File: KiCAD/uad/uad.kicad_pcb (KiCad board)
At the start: 2 copper layers, 100 x 70 mm, 77 parts, among them M3 ОтверстиеD3, X1 L_220, X2 N_220, X3 L_12, X4 N_12

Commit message: в общий проект добавлена лицевая панель под потенциометр
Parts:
- added G***: LOGO, N_ICO:el-nikitos_19x7, F.Cu at (116.5, 67.2)
- added M8: Отверстие_М8, N_X:Отверстие_М8, F.Cu at (95.2, 67.0)
- added XP10: Вилка_PLS3, N_X:Вилка_PLS3_угловая_вертикальная, B.Cu at (118.5, 62.2)
- added XP11: Вилка_PLS3, N_X:Вилка_PLS3_угловая_вертикальная, B.Cu at (118.5, 77.2)
- added XP8: Вилка_PLS3, N_X:Вилка_PLS3_угловая_вертикальная, B.Cu at (72.0, 56.8)
- added XP9: Вилка_PLS3, N_X:Вилка_PLS3_угловая_вертикальная, B.Cu at (72.0, 71.8)
- M3: value ОтверстиеD3 -> Отверстие_М3; footprint N_X:ОтверстиеD3 -> N_X:Отверстие_М3
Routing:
- net /uad_analog_panel/GND: track 0.00 -> 40.9 mm
- net /uad_analog_panel/VCC: track 0.00 -> 37.6 mm
- net /uad_analog_panel/BUT_COM_OUT: track 0.00 -> 9.92 mm
- net /uab_logic/GND: track 77.2 -> 74.0 mm, vias 12 -> 13
- net (no net): vias 0 -> 69
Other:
- board size 100 x 70 mm -> 100 x 100 mm
- board text added: "+12В(1)"
- board text added: "+12В(2)"
- board text added: "0"
- board text added: "0В(1)"
- board text added: "0В(2)"
- board text added: "1"
- board text added: "2"
- board text added: "3"
- board text added: "4"
- board text added: "5"
- board text added: "6"
- board text added: "7"
- board text added: "~~220В"
- board text added: "МАКС"
- board text added: "МИН"

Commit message: добавлены STEP и GERBER файлы
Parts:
- added C16: 100пФ(0603), N_RLC:Конденсатор_SMD_0603, B.Cu at (80.0, 142.8)
- added C17: 100пФ(0603), N_RLC:Конденсатор_SMD_0603, B.Cu at (131.5, 70.2)
- added C18: 100пФ(0603), N_RLC:Конденсатор_SMD_0603, B.Cu at (131.5, 59.8)
- added C19: 100пФ(0603), N_RLC:Конденсатор_SMD_0603, B.Cu at (94.2, 142.8)
- added C20: 100пФ(0603), N_RLC:Конденсатор_SMD_0603, B.Cu at (145.8, 70.2)
- added C21: 100пФ(0603), N_RLC:Конденсатор_SMD_0603, B.Cu at (145.8, 59.8)
- added C22: 100пФ(0603), N_RLC:Конденсатор_SMD_0603, B.Cu at (107.2, 142.8)
- added C23: 100пФ(0603), N_RLC:Конденсатор_SMD_0603, B.Cu at (158.8, 70.2)
- added C24: 100пФ(0603), N_RLC:Конденсатор_SMD_0603, B.Cu at (158.8, 59.8)
- added HL10: Светодиод_NeoPixel, N_VD_HL:Светодиод_SMD_neopixel_ws2812b, F.Cu at (72.8, 146.0)
- added HL11: Светодиод_NeoPixel, N_VD_HL:Светодиод_SMD_neopixel_ws2812b, F.Cu at (124.2, 73.5)
- added HL12: Светодиод_NeoPixel, N_VD_HL:Светодиод_SMD_neopixel_ws2812b, F.Cu at (124.2, 63.0)
- added HL13: Светодиод_NeoPixel, N_VD_HL:Светодиод_SMD_neopixel_ws2812b, F.Cu at (92.8, 146.0)
- added HL14: Светодиод_NeoPixel, N_VD_HL:Светодиод_SMD_neopixel_ws2812b, F.Cu at (144.2, 73.5)
- added HL15: Светодиод_NeoPixel, N_VD_HL:Светодиод_SMD_neopixel_ws2812b, F.Cu at (144.2, 63.0)
- added HL16: Светодиод_NeoPixel, N_VD_HL:Светодиод_SMD_neopixel_ws2812b, F.Cu at (112.5, 146.0)
- added HL17: Светодиод_NeoPixel, N_VD_HL:Светодиод_SMD_neopixel_ws2812b, F.Cu at (164.0, 73.5)
- added HL18: Светодиод_NeoPixel, N_VD_HL:Светодиод_SMD_neopixel_ws2812b, F.Cu at (164.0, 63.0)
- added M3: Отверстие_М3, N_X:Отверстие_М3, F.Cu at (85.5, 143.5)
- added M3: Отверстие_М3, N_X:Отверстие_М3, F.Cu at (137.0, 60.5)
- added M3: Отверстие_М3, N_X:Отверстие_М3, F.Cu at (137.0, 71.0)
- added XP12: Вилка_PLS3, N_X:Вилка_PLS3_угловая_вертикальная, B.Cu at (75.5, 146.0)
- added XP13: Вилка_PLS3, N_X:Вилка_PLS3_угловая_вертикальная, B.Cu at (127.0, 73.5)
- added XP14: Вилка_PLS3, N_X:Вилка_PLS3_угловая_вертикальная, B.Cu at (127.0, 63.0)
- added XP15: Вилка_PLS3, N_X:Вилка_PLS3_угловая_вертикальная, B.Cu at (113.0, 141.0)
- added XP16: Вилка_PLS3, N_X:Вилка_PLS3_угловая_вертикальная, B.Cu at (164.5, 68.5)
- added XP17: Вилка_PLS3, N_X:Вилка_PLS3_угловая_вертикальная, B.Cu at (164.5, 58.0)
- moved C10 0.71 mm to (155.2, 110.5)
- moved C11 0.71 mm to (150.0, 102.5)
- moved C12 0.71 mm to (150.8, 110.5)
- moved C13 0.71 mm to (129.8, 121.5)
- moved C14 0.71 mm to (129.8, 107.0)
- moved C15 0.71 mm to (137.0, 131.0)
- moved C9 0.71 mm to (154.5, 102.5)
- moved DD1 0.71 mm to (155.8, 107.2)
- moved FU1 0.71 mm to (167.0, 100.5)
- moved FU2 0.71 mm to (162.0, 134.5)
- moved G1 0.71 mm to (125.6, 133.6)
- moved HL1 0.71 mm to (144.0, 131.2)
- moved HL2 0.71 mm to (144.0, 127.0)
- moved HL3 0.71 mm to (129.0, 127.5)
- moved HL4 0.71 mm to (129.0, 112.5)
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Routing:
- net Net-(C16-Pad1): track 0.00 -> 60.8 mm, vias 0 -> 4
- net Net-(C18-Pad1): track 0.00 -> 59.8 mm, vias 0 -> 4
- net Net-(C17-Pad1): track 0.00 -> 59.8 mm, vias 0 -> 4
- net Net-(C18-Pad2): track 0.00 -> 51.9 mm, vias 0 -> 3
- net Net-(C17-Pad2): track 0.00 -> 51.9 mm, vias 0 -> 3
- net Net-(C16-Pad2): track 0.00 -> 51.9 mm, vias 0 -> 3
- net Net-(HL11-Pad2): track 0.00 -> 20.1 mm
- net Net-(HL12-Pad2): track 0.00 -> 20.1 mm
- net Net-(HL10-Pad2): track 0.00 -> 20.1 mm
- net Net-(HL15-Pad2): track 0.00 -> 18.6 mm
- net Net-(HL14-Pad2): track 0.00 -> 18.6 mm
- net Net-(HL13-Pad2): track 0.00 -> 18.6 mm
- net Net-(HL10-Pad4): track 0.00 -> 4.79 mm, vias 0 -> 1
- net Net-(HL12-Pad4): track 0.00 -> 4.79 mm, vias 0 -> 1
- net Net-(HL11-Pad4): track 0.00 -> 4.79 mm, vias 0 -> 1
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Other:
- board size 100 x 100 mm -> 99.5 x 100 mm
- board text added: "GND"
- board text added: "IN"
- board text added: "OUT"
- board text added: "VCC"
- board text added: "uad.0_1"
- board text added: "uad.0_2"
- board text added: "uad.0_3"

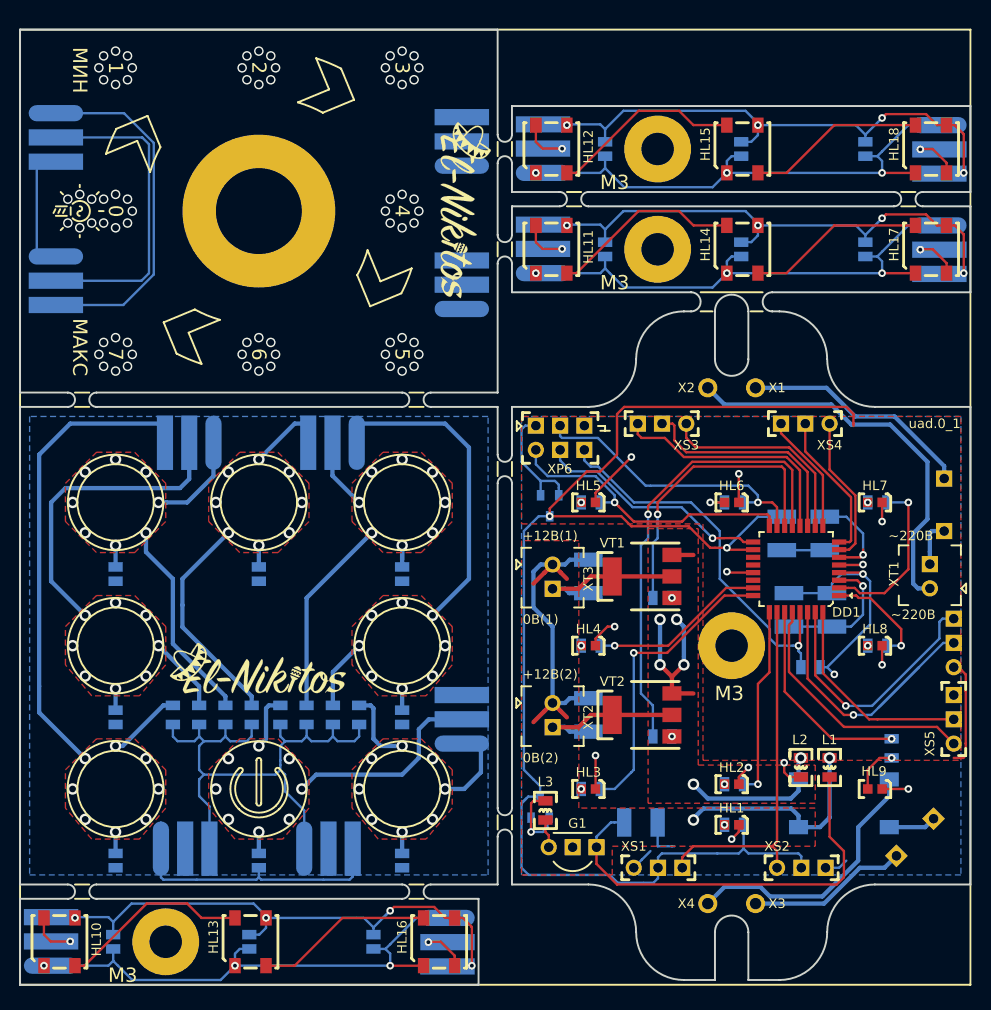
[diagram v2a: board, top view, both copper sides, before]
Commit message: убрана фигурная фрезеровка. заменены GERBER файлы
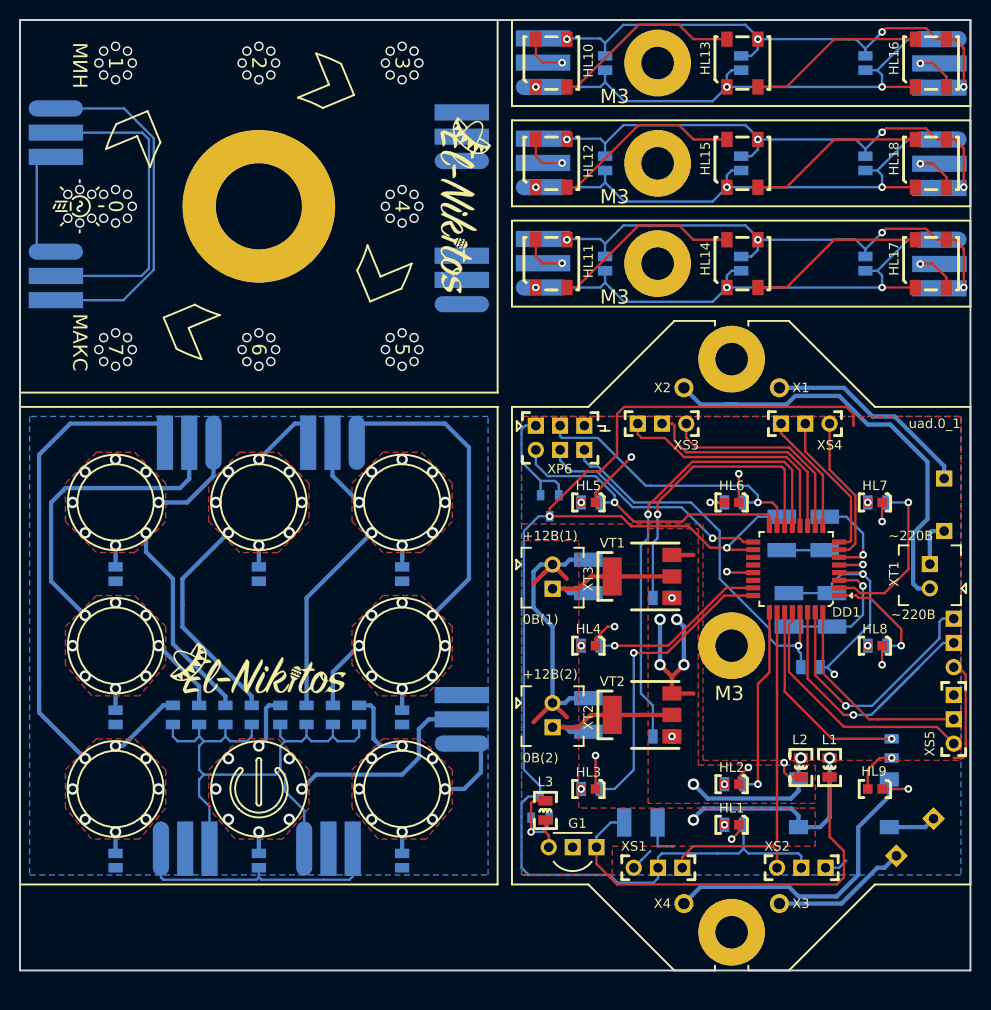
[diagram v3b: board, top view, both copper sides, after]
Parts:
- removed the M3 at (85.5, 143.5)
- removed the M3 at (137.0, 60.5)
- added M3: Отверстие_М3, N_X:Отверстие_М3, F.Cu at (137.0, 51.5)
- added M3: Отверстие_М3, N_X:Отверстие_М3, F.Cu at (144.8, 142.5)
- added M3: Отверстие_М3, N_X:Отверстие_М3, F.Cu at (144.8, 82.5)
- added M3: Отверстие_М3, N_X:Отверстие_М3, F.Cu at (137.0, 62.0)
- moved C16 105.4 mm to (131.5, 50.8)
- moved C19 105.4 mm to (145.8, 50.8)
- moved C22 105.4 mm to (158.8, 50.8)
- moved HL10 105.4 mm to (124.2, 54.0)
- moved HL13 105.4 mm to (144.2, 54.0)
- moved HL16 105.4 mm to (164.0, 54.0)
- moved XP12 105.4 mm to (127.0, 54.0)
- moved XP15 105.4 mm to (164.5, 49.0)
- moved X1 2.50 mm to (149.8, 85.5)
- moved X2 2.50 mm to (139.8, 85.5)
- moved X3 2.50 mm to (149.8, 139.5)
- moved X4 2.50 mm to (139.8, 139.5)
- moved C17 1.50 mm to (131.5, 71.8)
- moved C18 1.50 mm to (131.5, 61.2)
- moved C20 1.50 mm to (145.8, 71.8)
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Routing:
- net /uab_logic/N1: track 41.5 -> 46.0 mm
- net /uab_logic/N1_12: track 28.3 -> 31.7 mm
- net /uab_logic/L1_12: track 16.8 -> 14.3 mm
- net /uab_logic/L2: track 24.4 -> 21.9 mm
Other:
- board size 99.5 x 100 mm -> 99.5 x 99.5 mm

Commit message: начаты разворачиваться светодиоды
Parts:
- moved HL16 5.99 mm to (167.3, 49.0), turned to 270 degrees
- moved HL10 5.91 mm to (127.4, 49.0), turned to 270 degrees
- moved HL13 5.91 mm to (147.4, 49.0), turned to 270 degrees
- moved G1 0.40 mm to (125.6, 134.0)
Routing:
- net Net-(C15-Pad2): track 44.6 -> 46.9 mm
- net Net-(G1-Pad1): track 2.99 -> 4.24 mm
